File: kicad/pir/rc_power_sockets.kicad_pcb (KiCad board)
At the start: 2 copper layers, 50 x 50 mm, 31 parts, among them IC1 ATTINY85, J1 PIR, J2 433MHZ, J3 433MHZ, P1 ICSP, P2 ALT_PWR, Q1 NMOS, Q2 PMOS, U1 MCP1755ST-3302E/DB

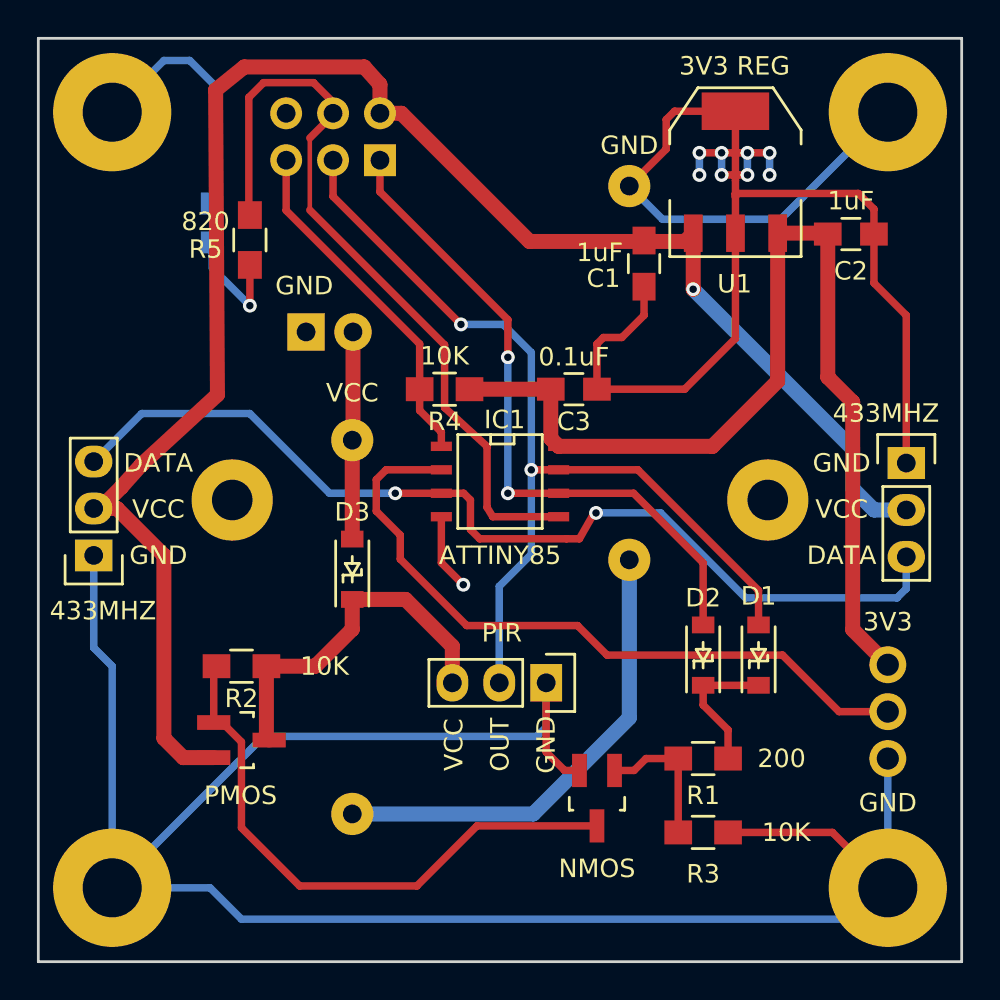
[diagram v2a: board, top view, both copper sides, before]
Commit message: Power switch
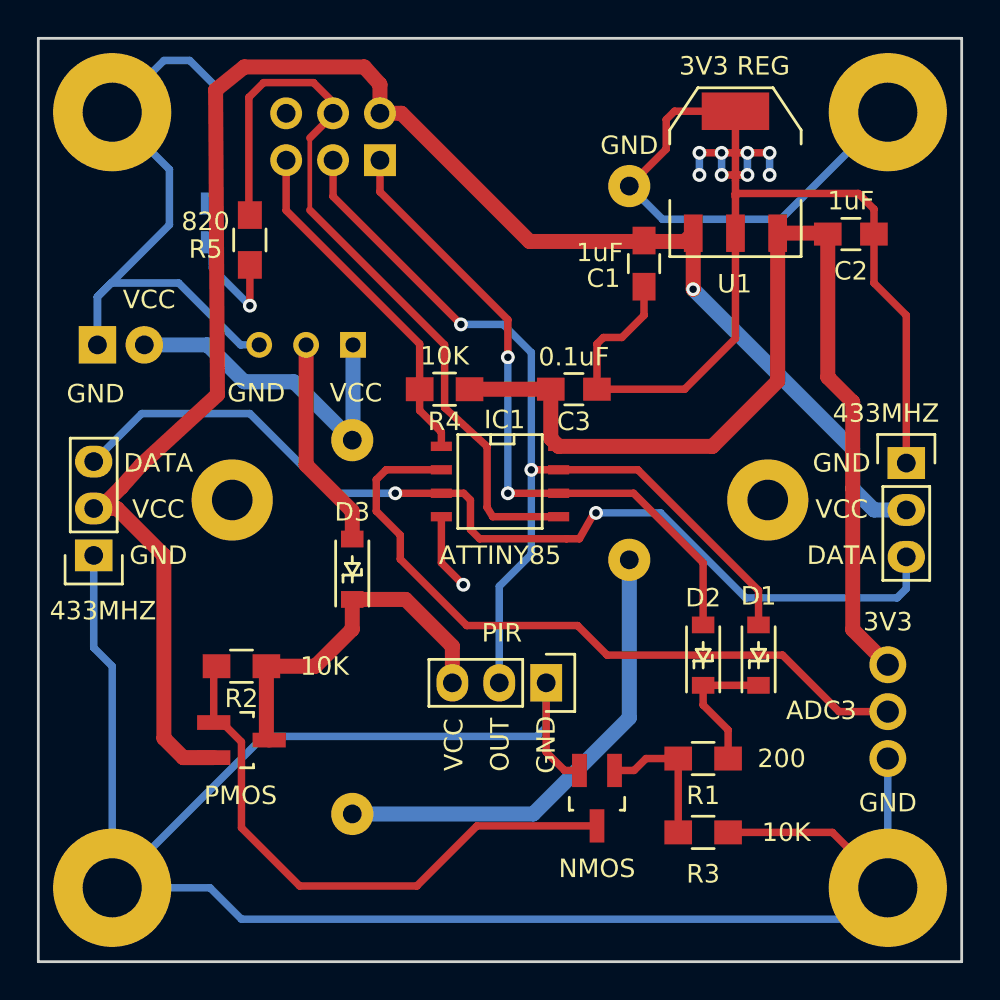
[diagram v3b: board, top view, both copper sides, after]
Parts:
- added SW1: SWITCH_INV, Buttons_Switches_ThroughHole:SW_Micro_SPST, B.Cu at (134.5, 76.6)
- moved P2 11.3 mm to (123.2, 76.6)
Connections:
- D3 pad 2: VCC -> /VCC_SWITCHED
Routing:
- net GND: track 221.4 -> 249.9 mm
- net /VCC_SWITCHED: track 0.00 -> 11.6 mm
- net VCC: track 11.6 -> 18.5 mm
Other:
- board text added: "ADC3"
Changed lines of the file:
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@@
 (kicad_pcb (version 4) (host pcbnew 4.0.2-4+6225~38~ubuntu14.04.1-stable)
   (general
-    (links 56)
+    (links 58)
     (no_connects 0)
-    (area 118.691667 58.475 171.675 111.375)
+    (area 119.924999 59.924999 170.075001 110.075001)
     (thickness 1.6)
-    (drawings 40)
-    (tracks 241)
+    (drawings 43)
+    (tracks 254)
     (zones 0)
-    (modules 31)
-    (nets 17)
+    (modules 32)
+    (nets 18)
   )
   (page A4)
@@
   (net 15 /BATT)
   (net 16 VCC)
+  (net 17 /VCC_SWITCHED)
   (net_class Default "This is the default net class."
     (clearance 0.2)
@@
     (add_net /POWER)
     (add_net /SWITCH_POWER)
+    (add_net /VCC_SWITCHED)
     (add_net VCC)
   )
@@
       (net 13 /POWER))
     (pad 2 smd rect (at 1.635 0 90) (size 0.91 1.22) (layers F.Cu F.Paste F.Mask)
-      (net 16 VCC))
+      (net 17 /VCC_SWITCHED))
   )
   (module theapi_footprints:LED_0805 (layer B.Cu)
@@
   )
   (module Pin_Headers:Pin_Header_Straight_1x02 (layer B.Cu)
-    (at 134.5 75.9 270)
+    (at 123.2 76.6 270)
     (descr "Through hole pin header")
     (tags "pin header")
@@
       (effects (font (size 1 1) (thickness 0.15)) (justify mirror))
     )
-    (fp_text value ALT_PWR (at 1 5 360) (layer B.SilkS)
+    (fp_text value ALT_PWR (at 2.8 -1.2 360) (layer B.SilkS)
       (effects (font (size 1 1) (thickness 0.15)) (justify mirror))
     )
@@
   (module theapi_footprints:CR2032H locked (layer B.Cu)
     (at 137 97 90)
-    (fp_text reference BT1 (at 0 12.7 90) (layer B.SilkS)
+    (fp_text reference BT1 (at 0 0 180) (layer B.SilkS)
       (effects (font (size 1 1) (thickness 0.15)) (justify mirror))
     )
@@
   (module theapi_footprints:CR2032H locked (layer B.Cu)
     (at 152 73 270)
-    (fp_text reference BT2 (at 0 12.7 270) (layer B.SilkS)
+    (fp_text reference BT2 (at -0.6 0 360) (layer B.SilkS)
       (effects (font (size 1 1) (thickness 0.15)) (justify mirror))
     )
@@
       (net 15 /BATT))
   )
+  (module Buttons_Switches_ThroughHole:SW_Micro_SPST (layer B.Cu)
+    (at 134.5 76.6 180)
+    (tags "Switch Micro SPST")
+    (fp_text reference SW1 (at 0 2.54 180) (layer B.SilkS)
+      (effects (font (size 1 1) (thickness 0.15)) (justify mirror))
+    )
+    (fp_text value SWITCH_INV (at 0.025 -2.45 180) (layer B.Fab)
+      (effects (font (size 1 1) (thickness 0.15)) (justify mirror))
+    )
+    (fp_line (start -3.81 -1.27) (end -3.81 1.27) (layer B.SilkS) (width 0.15))
+    (fp_line (start -3.81 1.27) (end 3.81 1.27) (layer B.SilkS) (width 0.15))
+    (fp_line (start 3.81 1.27) (end 3.81 -1.27) (layer B.SilkS) (width 0.15))
+    (fp_line (start 3.81 -1.27) (end -3.81 -1.27) (layer B.SilkS) (width 0.15))
+    (fp_line (start -1.27 1.27) (end -1.27 -1.27) (layer B.SilkS) (width 0.15))
+    (pad 1 thru_hole rect (at -2.54 0 180) (size 1.397 1.397) (drill 0.8128) (layers *.Cu *.Mask B.SilkS)
+      (net 16 VCC))
+    (pad 2 thru_hole circle (at 0 0 180) (size 1.397 1.397) (drill 0.8128) (layers *.Cu *.Mask B.SilkS)
+      (net 17 /VCC_SWITCHED))
+    (pad 3 thru_hole circle (at 2.54 0 180) (size 1.397 1.397) (drill 0.8128) (layers *.Cu *.Mask B.SilkS)
+      (net 1 GND))
+    (model Buttons_Switches_ThroughHole.3dshapes/SW_Micro_SPST.wrl
+      (at (xyz 0 0 0))
+      (scale (xyz 0.33 0.33 0.33))
+      (rotate (xyz 0 0 0))
+    )
+  )
+  (gr_text GND (at 131.8 79.2) (layer F.SilkS)
+    (effects (font (size 1 1) (thickness 0.15)))
+  )
+  (gr_text VCC (at 137.2 79.2) (layer F.SilkS)
+    (effects (font (size 1 1) (thickness 0.15)))
+  )
+  (gr_text ADC3 (at 162.4 96.4) (layer F.SilkS)
+    (effects (font (size 1 1) (thickness 0.15)))
+  )
   (gr_text 3V3 (at 166 91.6) (layer F.SilkS)
     (effects (font (size 1 1) (thickness 0.15)))
@@
     (effects (font (size 1 1) (thickness 0.15)) (justify mirror))
   )
-  (gr_text GND (at 134.4 73.4) (layer F.SilkS)
-    (effects (font (size 1 1) (thickness 0.15)))
-  )
-  (gr_text VCC (at 137 79.2) (layer F.SilkS)
-    (effects (font (size 1 1) (thickness 0.15)))
-  )
-  (gr_text GND (at 134.4 73.4) (layer B.SilkS)
+  (gr_text GND (at 123.1 79.25) (layer F.SilkS)
+    (effects (font (size 1 1) (thickness 0.15)))
+  )
+  (gr_text VCC (at 126 74.15) (layer F.SilkS)
+    (effects (font (size 1 1) (thickness 0.15)))
+  )
+  (gr_text GND (at 123.2 73.95) (layer B.SilkS)
     (effects (font (size 1 1) (thickness 0.15)) (justify mirror))
   )
@@
     (effects (font (size 1 1) (thickness 0.15) italic) (justify mirror))
   )
-  (gr_text VCC (at 137 78.25) (layer B.SilkS)
+  (gr_text VCC (at 139.95 76.65) (layer B.SilkS)
     (effects (font (size 1 1) (thickness 0.15)) (justify mirror))
   )
@@
   (gr_line (start 170 60) (end 170 110) (angle 90) (layer Edge.Cuts) (width 0.15))
   (gr_line (start 120 60) (end 170 60) (angle 90) (layer Edge.Cuts) (width 0.15))
+  (segment (start 131.96 76.6) (end 130.95 76.6) (width 0.406) (layer B.Cu) (net 1) (status 400000))
+  (segment (start 123.95 73.25) (end 123.2 74) (width 0.406) (layer B.Cu) (net 1))
+  (segment (start 127.6 73.25) (end 123.95 73.25) (width 0.406) (layer B.Cu) (net 1))
+  (segment (start 130.95 76.6) (end 127.6 73.25) (width 0.406) (layer B.Cu) (net 1))
+  (segment (start 123.2 74) (end 123.2 76.6) (width 0.406) (layer B.Cu) (net 1) (status 800000))
+  (segment (start 123.2 76.6) (end 123.2 74) (width 0.406) (layer B.Cu) (net 1))
+  (segment (start 127.1 67.1) (end 124 64) (width 0.406) (layer B.Cu) (net 1))
+  (segment (start 127.1 70.1) (end 127.1 67.1) (width 0.406) (layer B.Cu) (net 1))
+  (segment (start 123.2 74) (end 127.1 70.1) (width 0.406) (layer B.Cu) (net 1))
   (segment (start 152 68) (end 153.8 69.8) (width 0.406) (layer B.Cu) (net 1))
   (segment (start 160.2 69.8) (end 166 64) (width 0.406) (layer B.Cu) (net 1))
@@
   (segment (start 146.8 102) (end 137 102) (width 0.813) (layer B.Cu) (net 15))
   (segment (start 152 96.8) (end 146.8 102) (width 0.813) (layer B.Cu) (net 15))
-  (segment (start 137.04 75.9) (end 137.04 81.72) (width 0.813) (layer F.Cu) (net 16))
-  (segment (start 137.04 81.72) (end 137 81.76) (width 0.813) (layer F.Cu) (net 16))
-  (segment (start 136.75 81.51) (end 137 81.76) (width 0.813) (layer F.Cu) (net 16))
-  (segment (start 137 87.115) (end 137 81.76) (width 0.813) (layer F.Cu) (net 16))
+  (segment (start 125.74 76.6) (end 129.15 76.6) (width 0.813) (layer B.Cu) (net 16) (status 400000))
+  (segment (start 133.84 78.6) (end 137 81.76) (width 0.813) (layer B.Cu) (net 16) (status 800000))
+  (segment (start 131.15 78.6) (end 133.84 78.6) (width 0.813) (layer B.Cu) (net 16))
+  (segment (start 129.15 76.6) (end 131.15 78.6) (width 0.813) (layer B.Cu) (net 16))
+  (segment (start 137.04 76.6) (end 137.04 81.72) (width 0.813) (layer B.Cu) (net 16))
+  (segment (start 134.5 76.6) (end 134.5 83.1) (width 0.813) (layer F.Cu) (net 17))
+  (segment (start 137 85.6) (end 137 87.115) (width 0.813) (layer F.Cu) (net 17))
+  (segment (start 134.5 83.1) (end 137 85.6) (width 0.813) (layer F.Cu) (net 17))
   (zone (net 1) (net_name GND) (layer B.Cu) (hatch edge 0.508)
     (connect_pads (clearance 0.508))

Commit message: Moved the led
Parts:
- R5: moved to B.Cu
- moved D4 38.7 mm to (168.0, 72.9)
- moved R5 34.1 mm to (165.5, 72.9)
- moved SW1 5.45 mm to (130.5, 72.9)
- moved P2 2.71 mm to (123.0, 73.9), turned to 180 degrees
- moved C3 0.81 mm to (149.4, 79.7)
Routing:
- net GND: track 249.9 -> 279.0 mm
- net /MOSI: track 42.4 -> 56.2 mm, vias 0 -> 1
- net /VCC_SWITCHED: track 11.6 -> 16.9 mm
- net Net-(D4-Pad2): track 6.47 -> 2.62 mm, vias 1 -> 0
- net VCC: track 18.5 -> 22.2 mm
- net /RESET: track 19.0 -> 21.6 mm
- net /SWITCH_POWER: track 95.7 -> 97.7 mm
- net /SCK: track 52.1 -> 53.8 mm
- net /MISO: track 36.4 -> 37.5 mm
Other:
- board text added: "OFF"
- board text added: "ON"

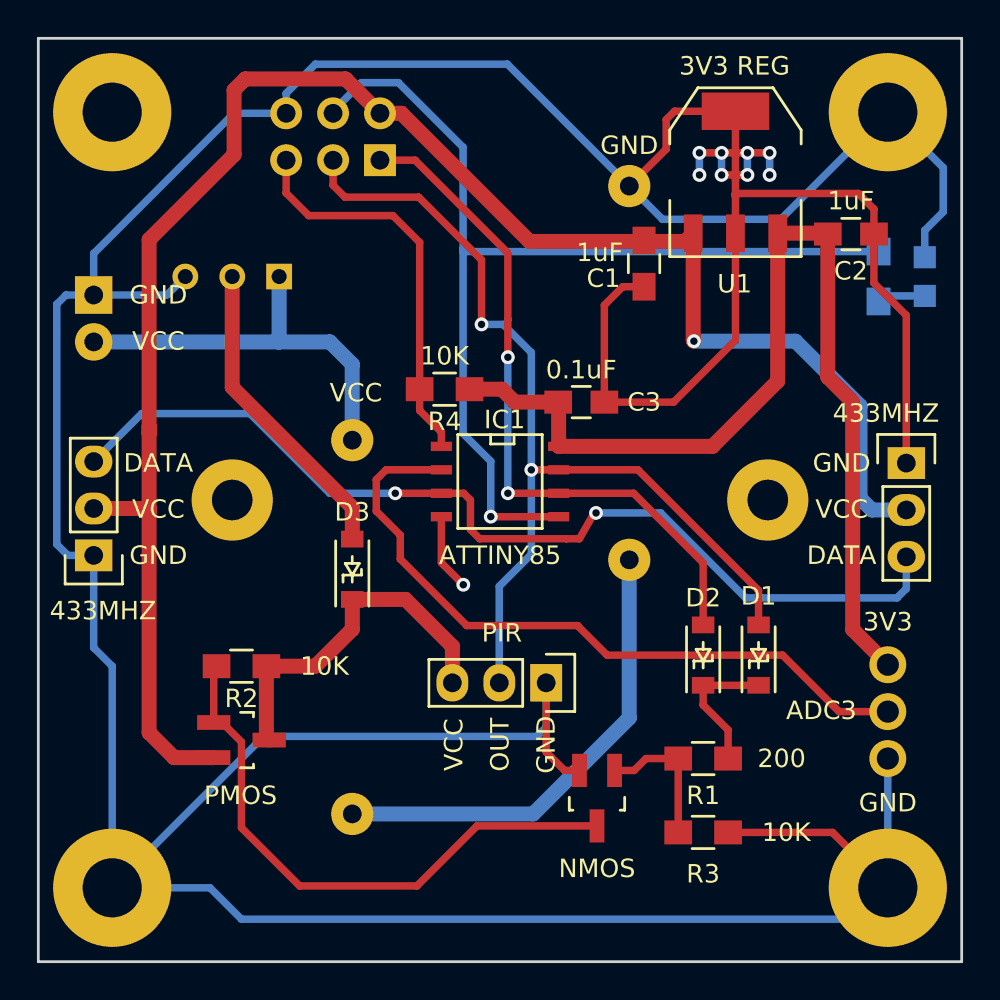
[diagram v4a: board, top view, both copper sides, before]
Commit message: Moved components out of the way of parts on the PIR
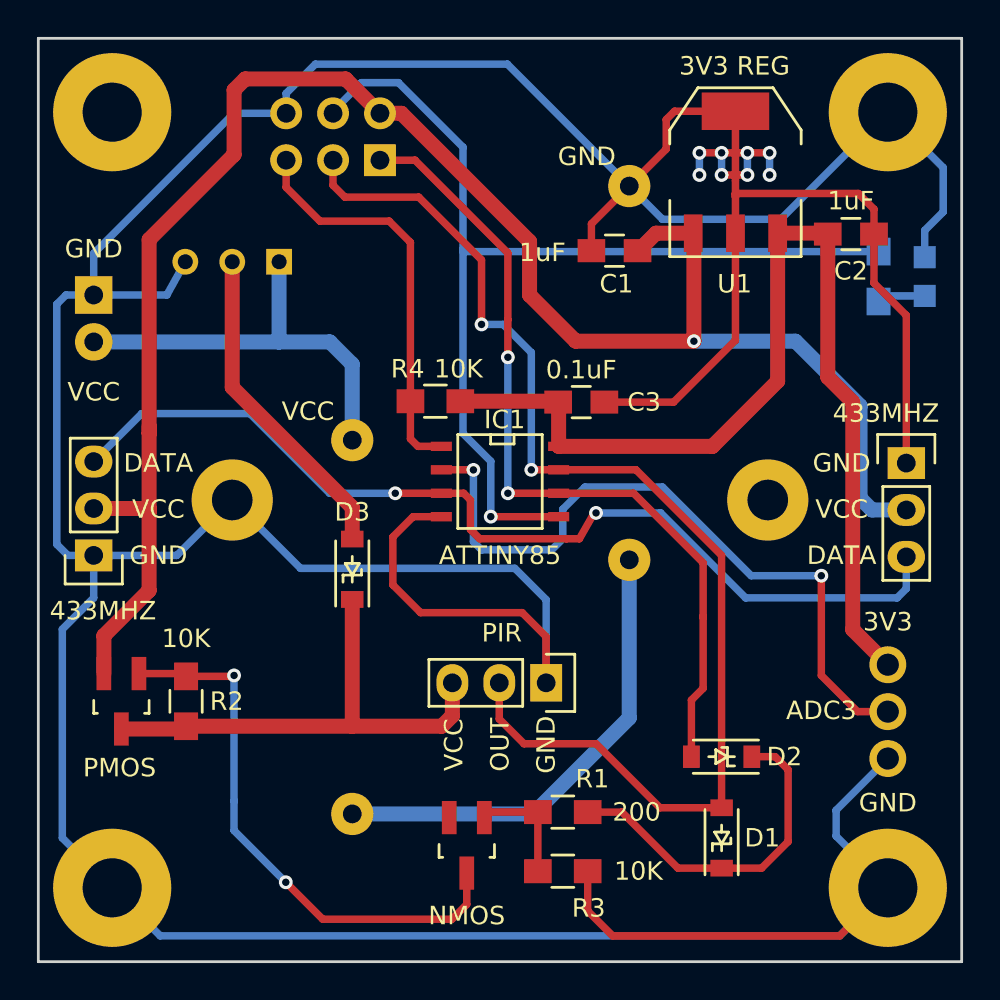
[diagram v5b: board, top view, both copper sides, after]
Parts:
- moved D1 10.1 mm to (157.0, 103.3)
- moved R1 8.13 mm to (148.4, 101.9)
- moved R3 7.88 mm to (148.4, 105.1)
- moved Q1 7.50 mm to (143.2, 103.7)
- moved Q2 6.83 mm to (124.5, 95.9), turned to 180 degrees
- moved D2 5.59 mm to (157.0, 98.9), turned to 180 degrees
- moved R2 3.55 mm to (128.0, 95.9), turned to 90 degrees
- moved C1 1.75 mm to (151.2, 71.5), turned to 180 degrees
- moved R4 0.82 mm to (141.5, 79.7)
- moved SW1 0.80 mm to (130.5, 72.1)
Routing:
- net GND: track 279.0 -> 301.1 mm, vias 9 -> 8
- net /SCK: track 53.8 -> 66.1 mm
- net /NBASE_ON: track 9.01 -> 18.9 mm
- net /MISO: track 37.5 -> 45.0 mm
- net /POWER: track 19.7 -> 27.2 mm
- net /PBASE: track 32.6 -> 30.3 mm, vias 0 -> 2
- net /NBASE: track 7.72 -> 6.22 mm
- net /SWITCH_POWER: track 97.7 -> 98.8 mm
- net VCC: track 22.2 -> 23.0 mm
- net /VCC_SWITCHED: track 16.9 -> 17.7 mm
- net /ADC3: track 38.4 -> 38.8 mm, vias 0 -> 2
